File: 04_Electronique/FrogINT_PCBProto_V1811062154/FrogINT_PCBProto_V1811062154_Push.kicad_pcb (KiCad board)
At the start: 2 copper layers, 100 x 100 mm, 32 parts, among them J1 USB_B_Mini, J2 Conn_01x01_Female, J3 AVR-JTAG-10, Q1 PMV48XP, Q2 PMV48XP, SW1 SW_SPST, SW2 SW_SPST, U1 NCP1117-5.0_SOT223, U2 LP2985-3.3, U3 ATmega16U4RC-AU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

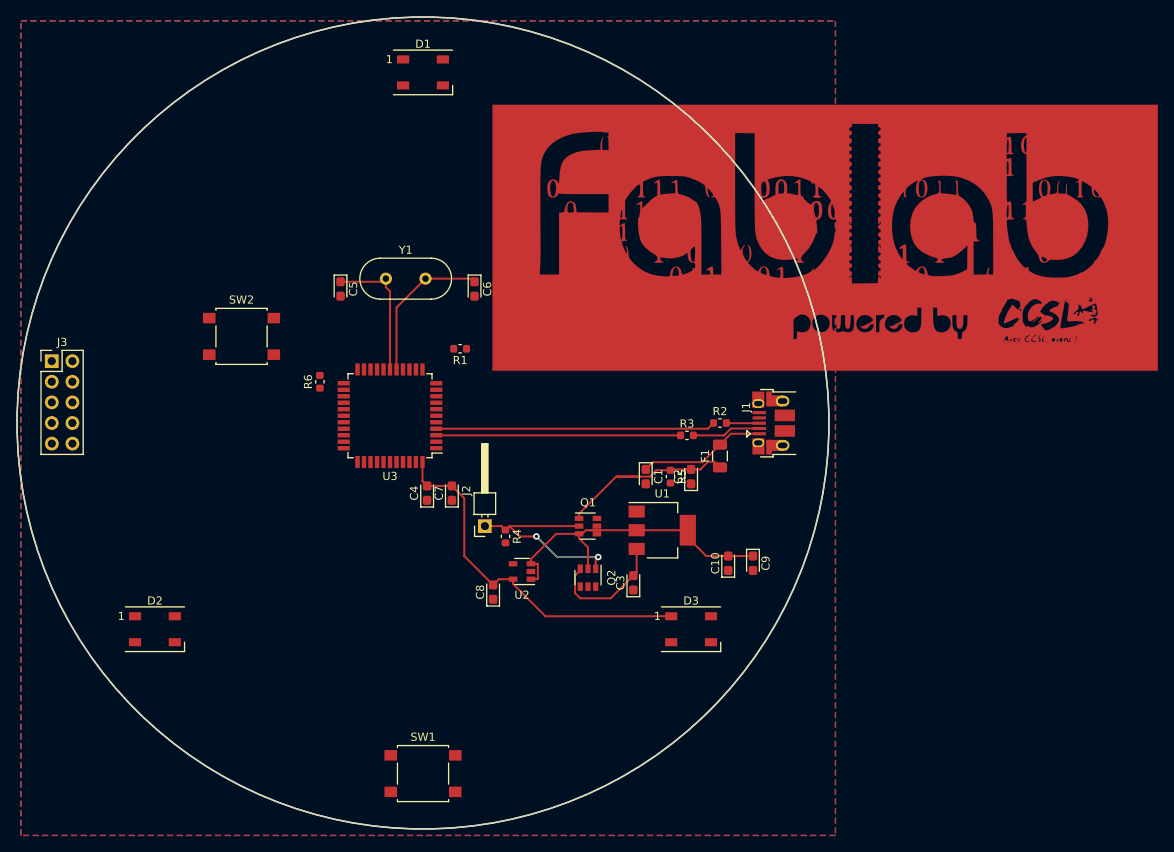
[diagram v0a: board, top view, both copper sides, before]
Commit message: Ajout d'un Logo-FrogINT en tant qu'Image et que module pour l'inclure sur le PCB et SilkScreen
Ajout d'une version "Push" du PCB avec l'utilisation de Freerouting - autoroutage.
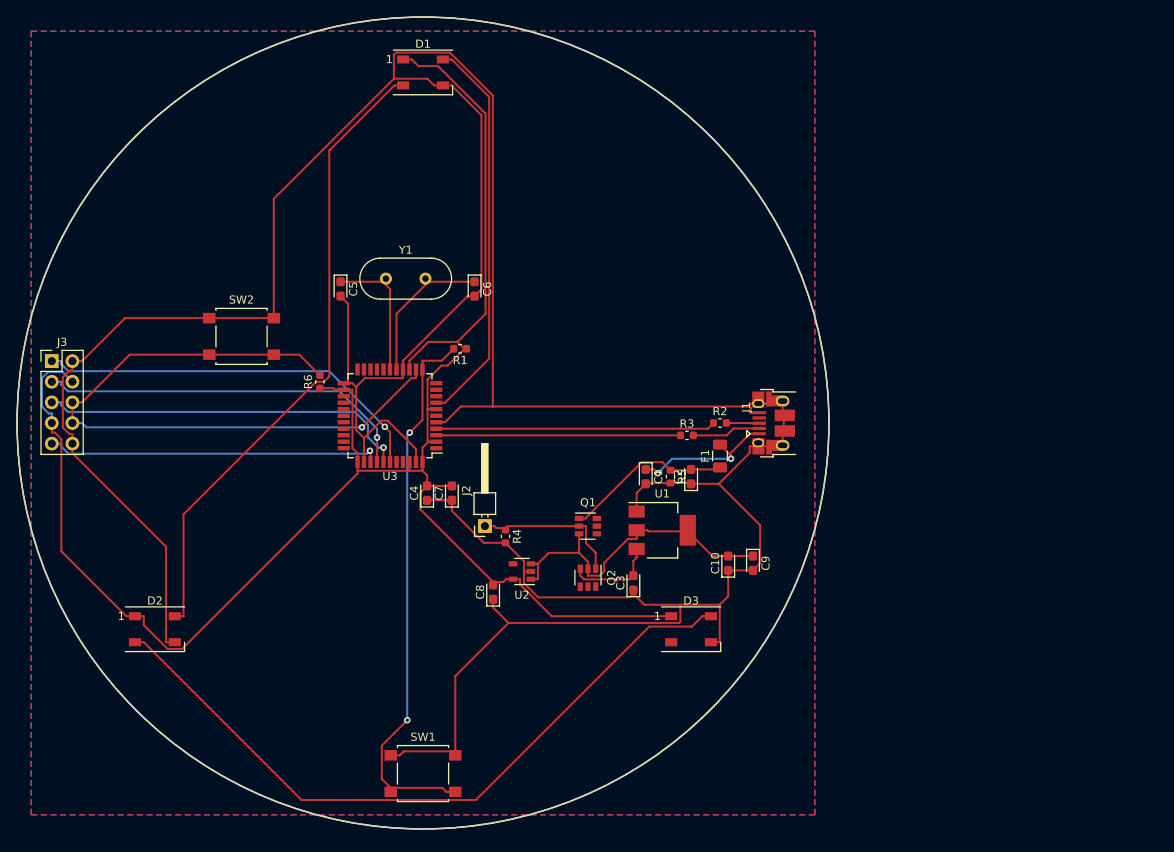
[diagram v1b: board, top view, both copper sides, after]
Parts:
- removed G***: LOGO, FTA_FrogINT_Library_Footprint_Package:Logo_FabLab_Copper
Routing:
- net GND: track 0.00 -> 453.0 mm
- net +3V3: track 45.0 -> 219.5 mm
- net Net-(D2-Pad2): track 0.00 -> 88.4 mm
- net /reset: track 0.00 -> 82.6 mm, vias 0 -> 1
- net Net-(D1-Pad2): track 0.00 -> 78.9 mm
- net /Input_Interrupt: track 0.00 -> 68.2 mm, vias 0 -> 2
- net Net-(J3-Pad1): track 0.00 -> 49.2 mm, vias 0 -> 1
- net Net-(D1-Pad4): track 0.00 -> 48.6 mm
- net Net-(J3-Pad3): track 0.00 -> 46.8 mm, vias 0 -> 1
- net Net-(J3-Pad5): track 0.00 -> 46.0 mm, vias 0 -> 1
- net Net-(J3-Pad9): track 0.00 -> 41.5 mm, vias 0 -> 1
- net /Vin: track 26.1 -> 18.6 mm, vias 2 -> 0
- net Net-(C3-Pad2): track 15.3 -> 11.2 mm
- net VBUS: track 23.7 -> 20.8 mm
- net Net-(C1-Pad1): track 15.8 -> 18.4 mm, vias 0 -> 2
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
